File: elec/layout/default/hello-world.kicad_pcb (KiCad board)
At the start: 2 copper layers, 105 x 88 mm, 319 parts, among them Q1 ?, Q2 ?, U1 ?, U2 ?, U3 ?, U4 ?

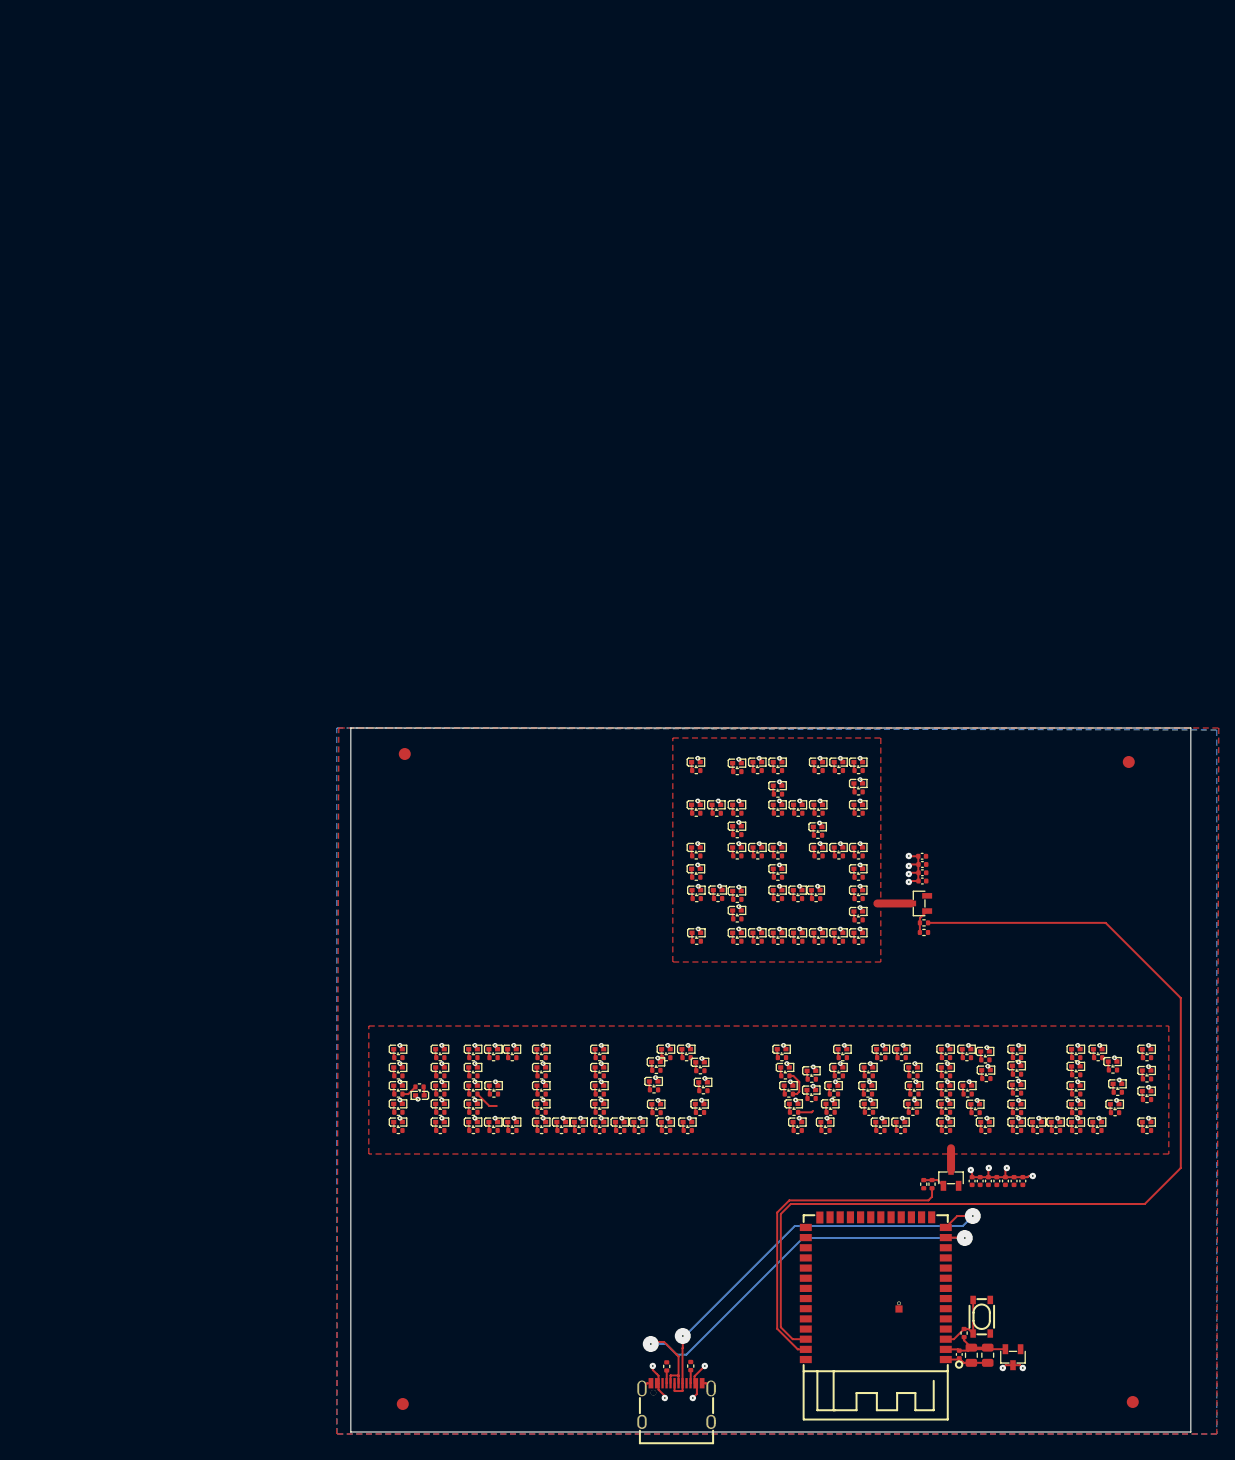
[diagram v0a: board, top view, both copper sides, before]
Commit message: rotat 90 degrees and move to kicad X0Y0
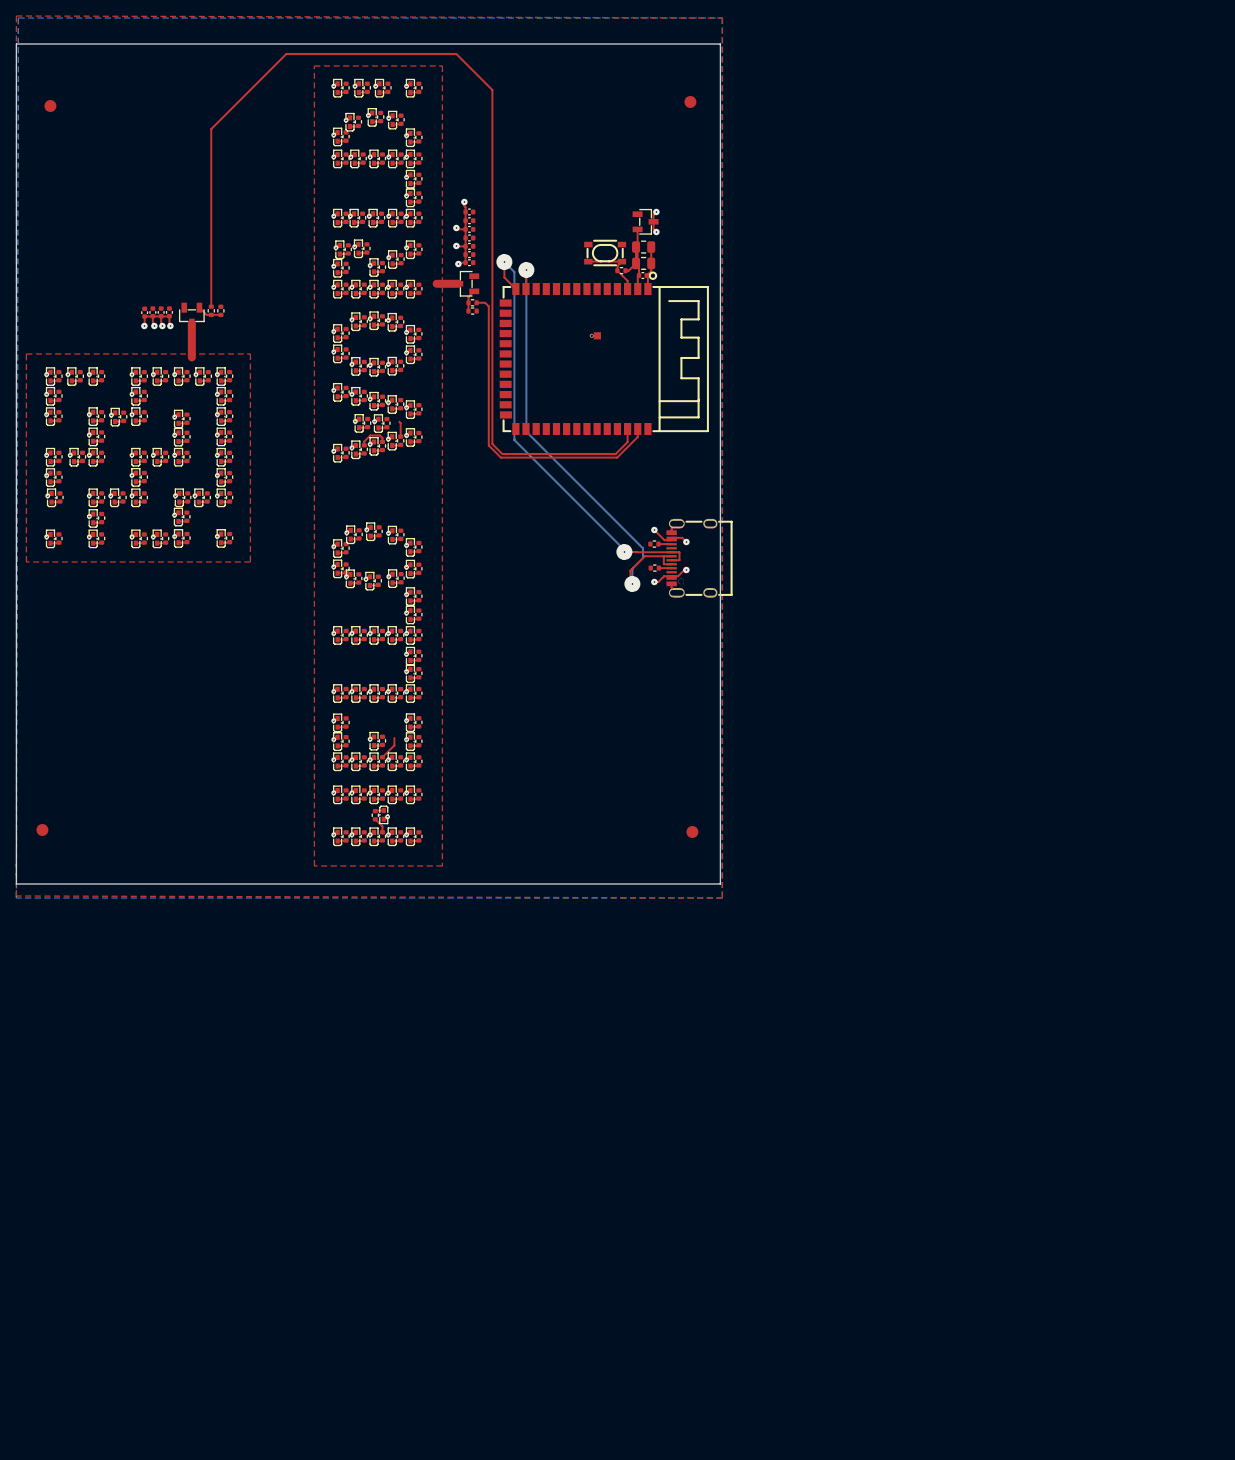
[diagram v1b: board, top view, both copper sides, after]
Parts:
- moved FID1 171.7 mm to (84.2, 10.5), turned to 90 degrees
- moved R70 159.0 mm to (50.3, 8.73), turned to 90 degrees
- moved LED63 158.7 mm to (49.2, 8.77), turned to 90 degrees
- moved R103 158.1 mm to (46.4, 8.73), turned to 90 degrees
- moved LED96 157.8 mm to (45.3, 8.77), turned to 90 degrees
- moved FID4 157.8 mm to (4.20, 11.0), turned to 90 degrees
- moved R54 157.6 mm to (43.8, 8.73), turned to 90 degrees
- moved LED47 157.4 mm to (42.8, 8.77), turned to 90 degrees
- moved R29 157.2 mm to (41.2, 8.73), turned to 90 degrees
- moved LED22 157.0 mm to (40.1, 8.77), turned to 90 degrees
- moved R105 152.9 mm to (48.0, 12.7), turned to 90 degrees
- moved R77 152.8 mm to (45.5, 12.4), turned to 90 degrees
- moved LED98 152.6 mm to (47.0, 12.8), turned to 90 degrees
- moved LED70 152.5 mm to (44.4, 12.4), turned to 90 degrees
- moved R34 151.5 mm to (42.7, 13.0), turned to 90 degrees
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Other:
- board size 105 x 88 mm -> 88 x 105 mm
- board text removed: "HELLO WORLD!"
